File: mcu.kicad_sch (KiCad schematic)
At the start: 51 parts, among them IC3 RP2040, U1 W25Q64JVZPIQ, Y1 ABM3B-12.000MHZ-10-1-U-T

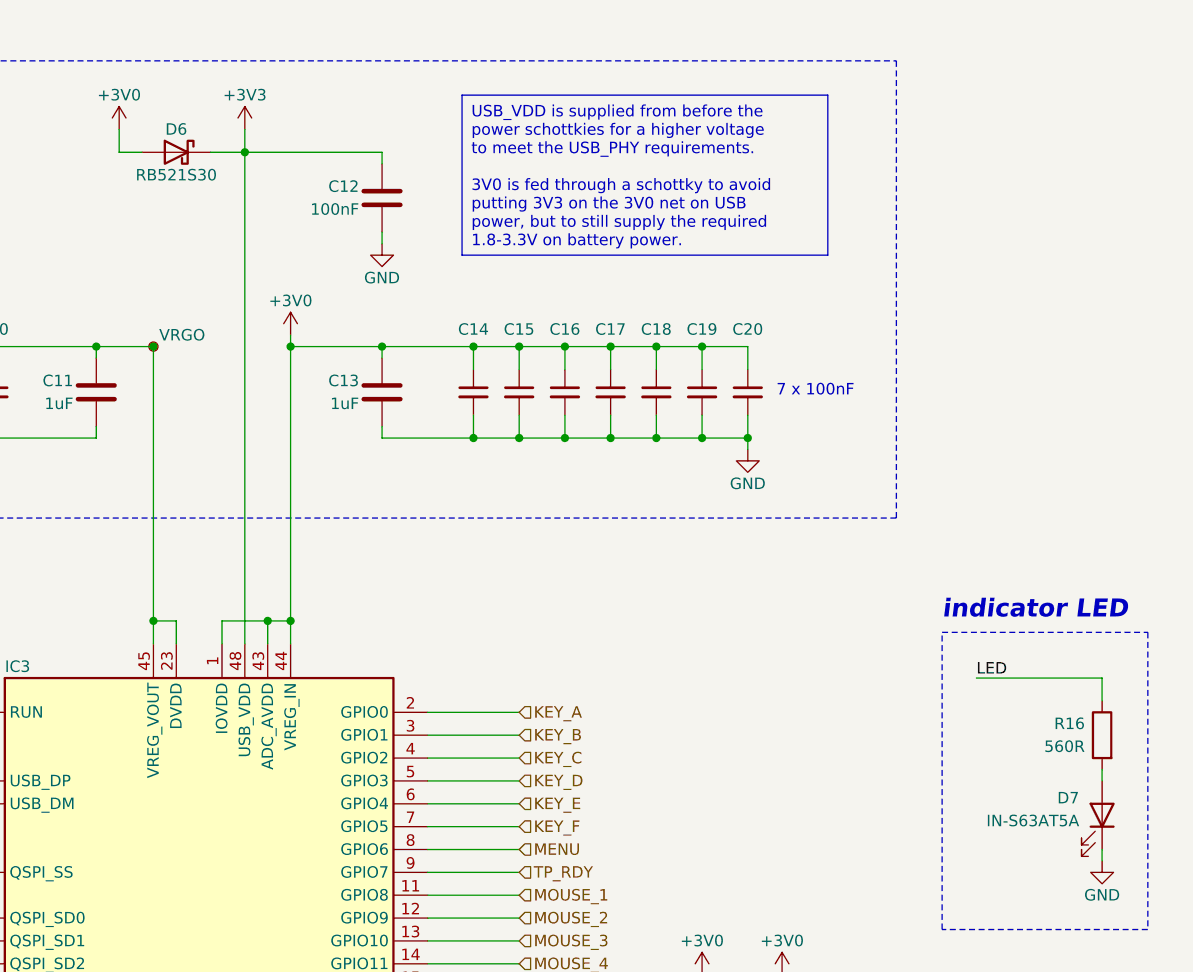
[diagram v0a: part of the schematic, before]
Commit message: add second battery TVS
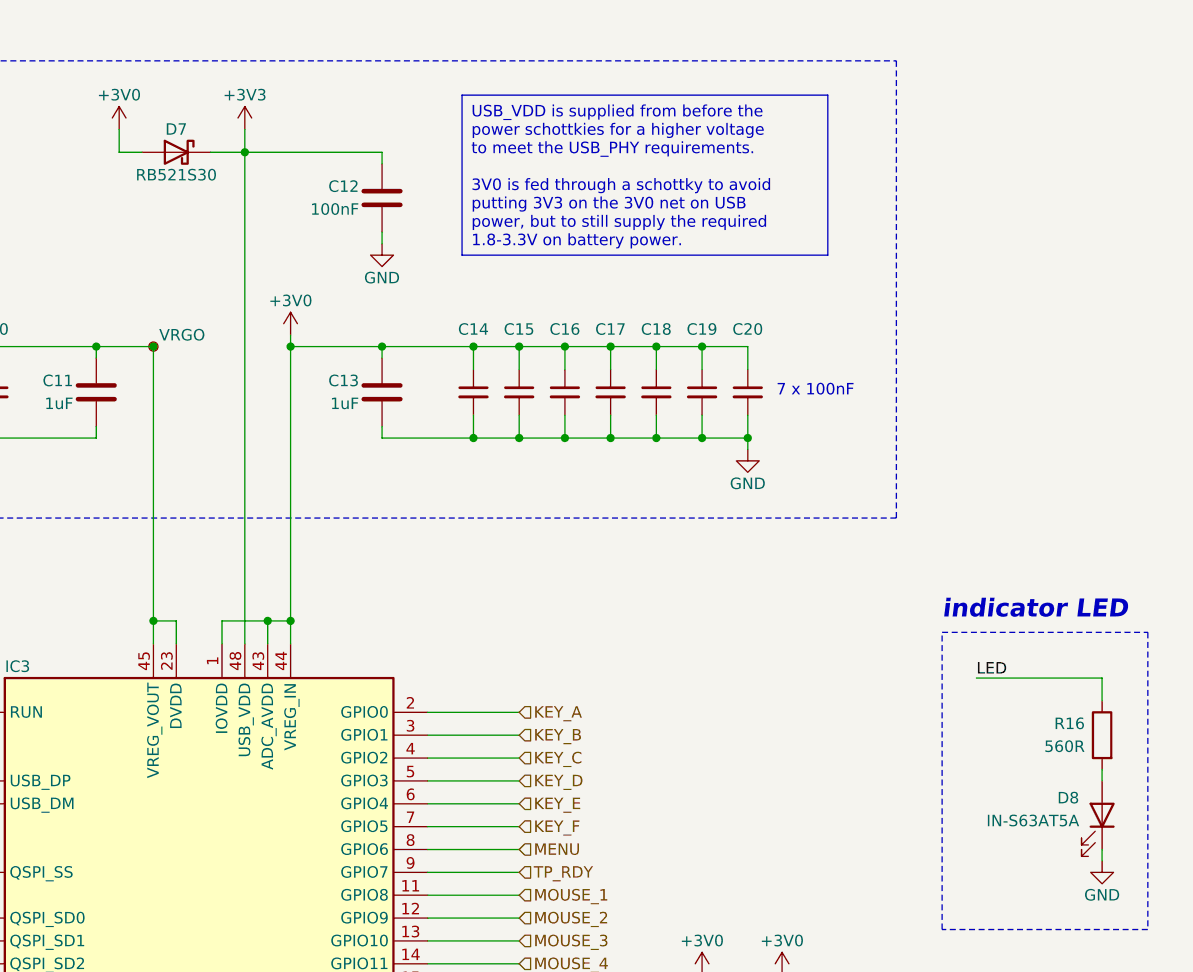
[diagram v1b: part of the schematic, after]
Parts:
- renumbered D6 to D7, D7 to D8
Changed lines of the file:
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@@
   (symbol (lib_id "user:RB521S30") (at 165.1 35.56 0) (mirror y) (unit 1)
     (in_bom yes) (on_board yes) (dnp no)
-    (property "Reference" "D6" (at 165.1 33.02 0)
+    (property "Reference" "D7" (at 165.1 33.02 0)
       (effects (font (size 1.27 1.27)))
     )
@@
       (project "gkos_pebble"
         (path "/ab6fff6e-44fa-4992-ab9d-8d9a7df4367d/b094ad32-9f85-443d-ad4d-e6b703944261"
-          (reference "D6") (unit 1)
+          (reference "D7") (unit 1)
         )
       )
@@
   (symbol (lib_id "Device:LED") (at 267.97 109.22 270) (mirror x) (unit 1)
     (in_bom yes) (on_board yes) (dnp no)
-    (property "Reference" "D7" (at 265.43 107.315 90)
+    (property "Reference" "D8" (at 265.43 107.315 90)
       (effects (font (size 1.27 1.27)) (justify right))
     )
@@
       (project "gkos_pebble"
         (path "/ab6fff6e-44fa-4992-ab9d-8d9a7df4367d/b094ad32-9f85-443d-ad4d-e6b703944261"
-          (reference "D7") (unit 1)
-        )
-      )
+          (reference "D8") (unit 1)
+        )
+      )

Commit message: add one more battery TVS
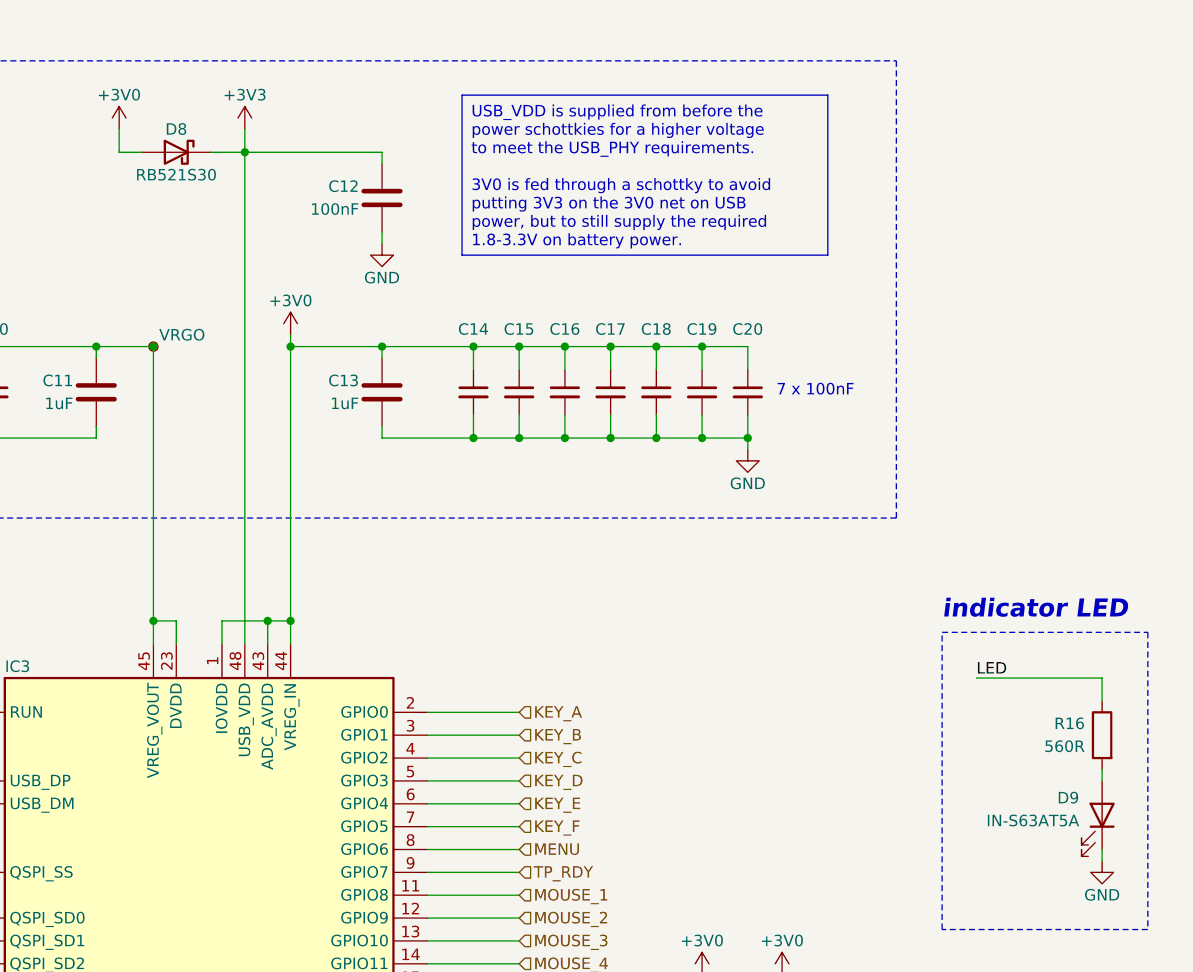
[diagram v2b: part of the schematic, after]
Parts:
- renumbered D7 to D8, D8 to D9
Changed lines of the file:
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@@
   (symbol (lib_id "user:RB521S30") (at 165.1 35.56 0) (mirror y) (unit 1)
     (in_bom yes) (on_board yes) (dnp no)
-    (property "Reference" "D7" (at 165.1 33.02 0)
+    (property "Reference" "D8" (at 165.1 33.02 0)
       (effects (font (size 1.27 1.27)))
     )
@@
       (project "gkos_pebble"
         (path "/ab6fff6e-44fa-4992-ab9d-8d9a7df4367d/b094ad32-9f85-443d-ad4d-e6b703944261"
-          (reference "D7") (unit 1)
+          (reference "D8") (unit 1)
         )
       )
@@
   (symbol (lib_id "Device:LED") (at 267.97 109.22 270) (mirror x) (unit 1)
     (in_bom yes) (on_board yes) (dnp no)
-    (property "Reference" "D8" (at 265.43 107.315 90)
+    (property "Reference" "D9" (at 265.43 107.315 90)
       (effects (font (size 1.27 1.27)) (justify right))
     )
@@
       (project "gkos_pebble"
         (path "/ab6fff6e-44fa-4992-ab9d-8d9a7df4367d/b094ad32-9f85-443d-ad4d-e6b703944261"
-          (reference "D8") (unit 1)
-        )
-      )
+          (reference "D9") (unit 1)
+        )
+      )

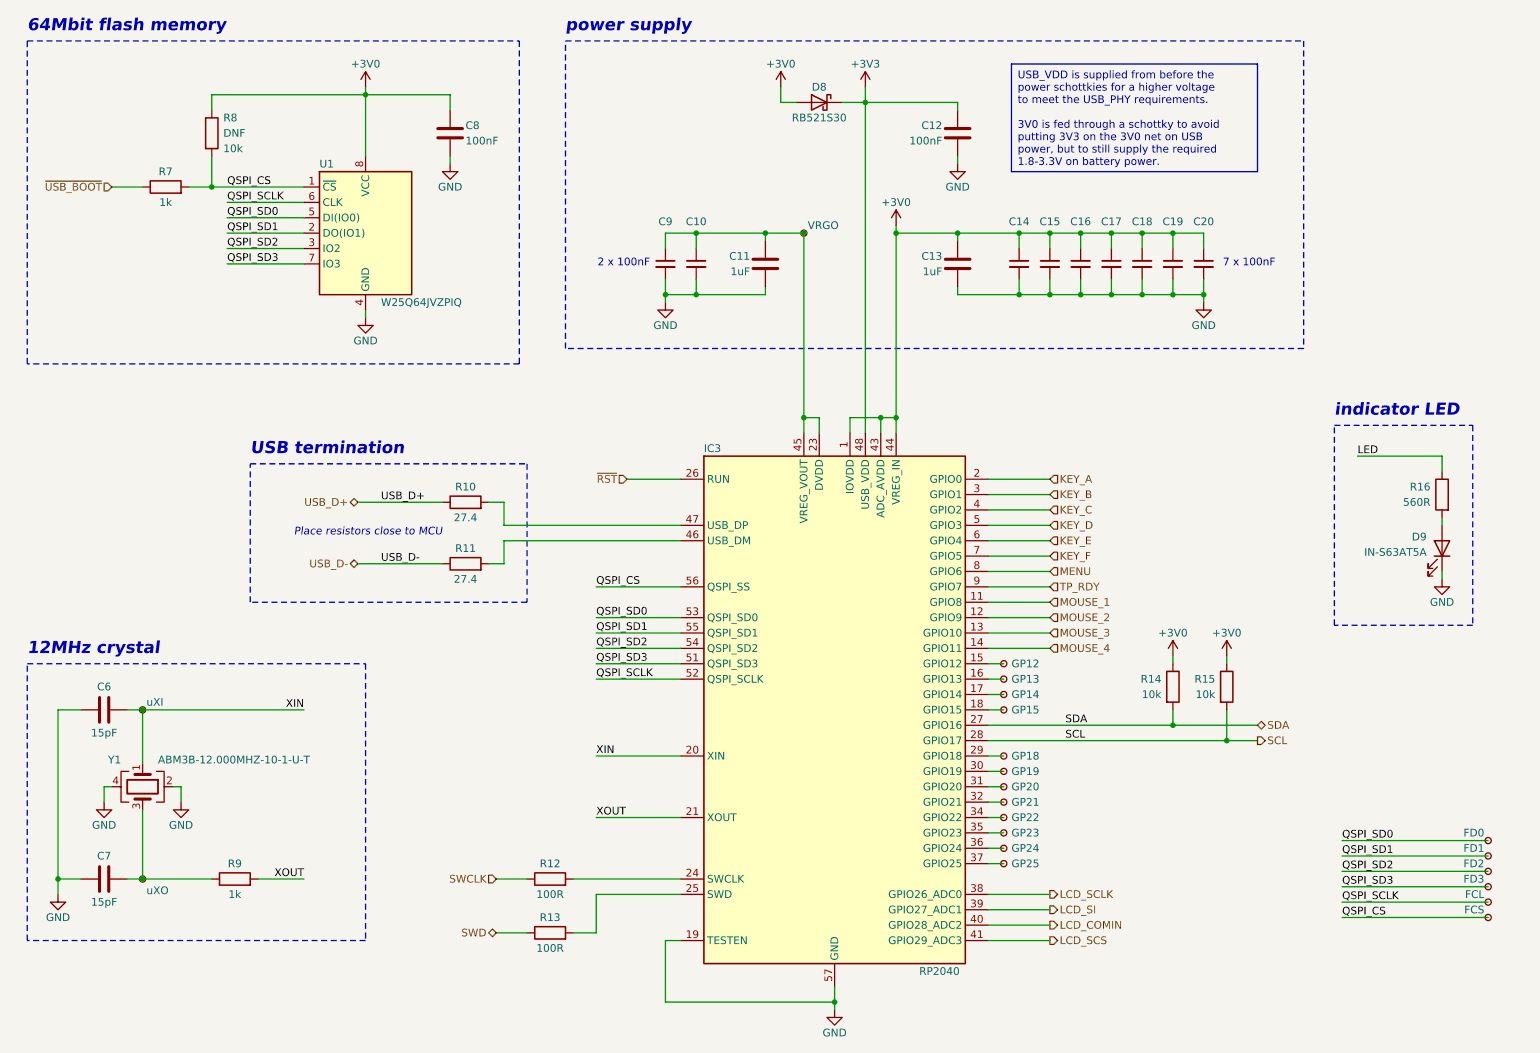
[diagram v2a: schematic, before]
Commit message: add the dang eeprom
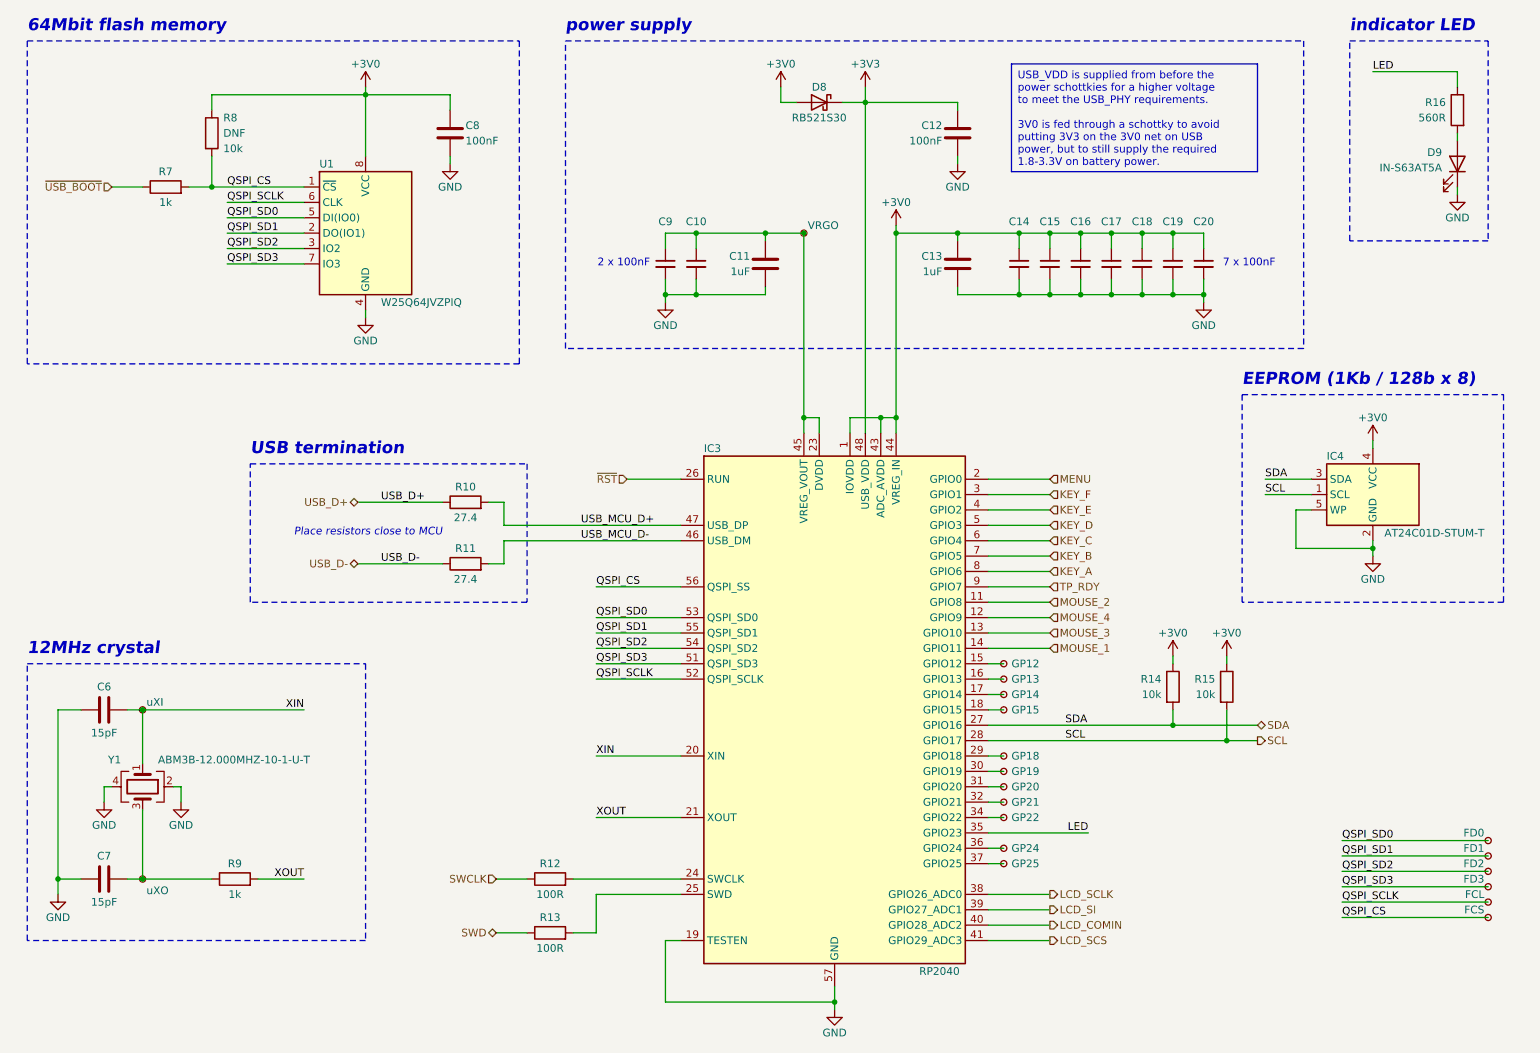
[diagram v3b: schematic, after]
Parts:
- removed TP40: GP23, TestPoint:TestPoint_Pad_D1.0mm, symbol Connector:TestPoint_Small
- added IC4: AT24C01D-STUM-T, Package_TO_SOT_SMD:SOT-23-5, symbol Memory_EEPROM:AT24CS01-STUM
- renumbered TP41 to TP40, TP42 to TP41, TP43 to TP42, TP44 to TP43, TP45 to TP44, TP46 to TP45, TP47 to TP46, TP48 to TP47
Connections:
- net +3V0: now also IC4.4 (VCC)
- net GND: now also IC4.2 (GND), IC4.5 (WP)
- net KEY_A: now also IC3.8 (GPIO6); no longer IC3.2 (GPIO0)
- net KEY_B: now also IC3.7 (GPIO5); no longer IC3.3 (GPIO1)
- net KEY_C: now also IC3.6 (GPIO4); no longer IC3.4 (GPIO2)
- net KEY_E: now also IC3.4 (GPIO2); no longer IC3.6 (GPIO4)
- net KEY_F: now also IC3.3 (GPIO1); no longer IC3.7 (GPIO5)
- net LED: now also IC3.35 (GPIO23)
- net MENU: now also IC3.2 (GPIO0); no longer IC3.8 (GPIO6)
- net MOUSE_1: now also IC3.14 (GPIO11); no longer IC3.11 (GPIO8)
- net MOUSE_2: now also IC3.11 (GPIO8); no longer IC3.12 (GPIO9)
- net MOUSE_4: now also IC3.12 (GPIO9); no longer IC3.14 (GPIO11)
- net SCL: now also IC4.1 (SCL)
- net SDA: now also IC4.3 (SDA)
- net USB_MCU_D+: now reaches IC3.47 (USB_DP), R10.2
- net USB_MCU_D-: now reaches IC3.46 (USB_DM), R11.2
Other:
- note added: "EEPROM (1Kb / 128b x 8)"
- moved on the sheet: D9, R16

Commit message: swap crystal for smaller one
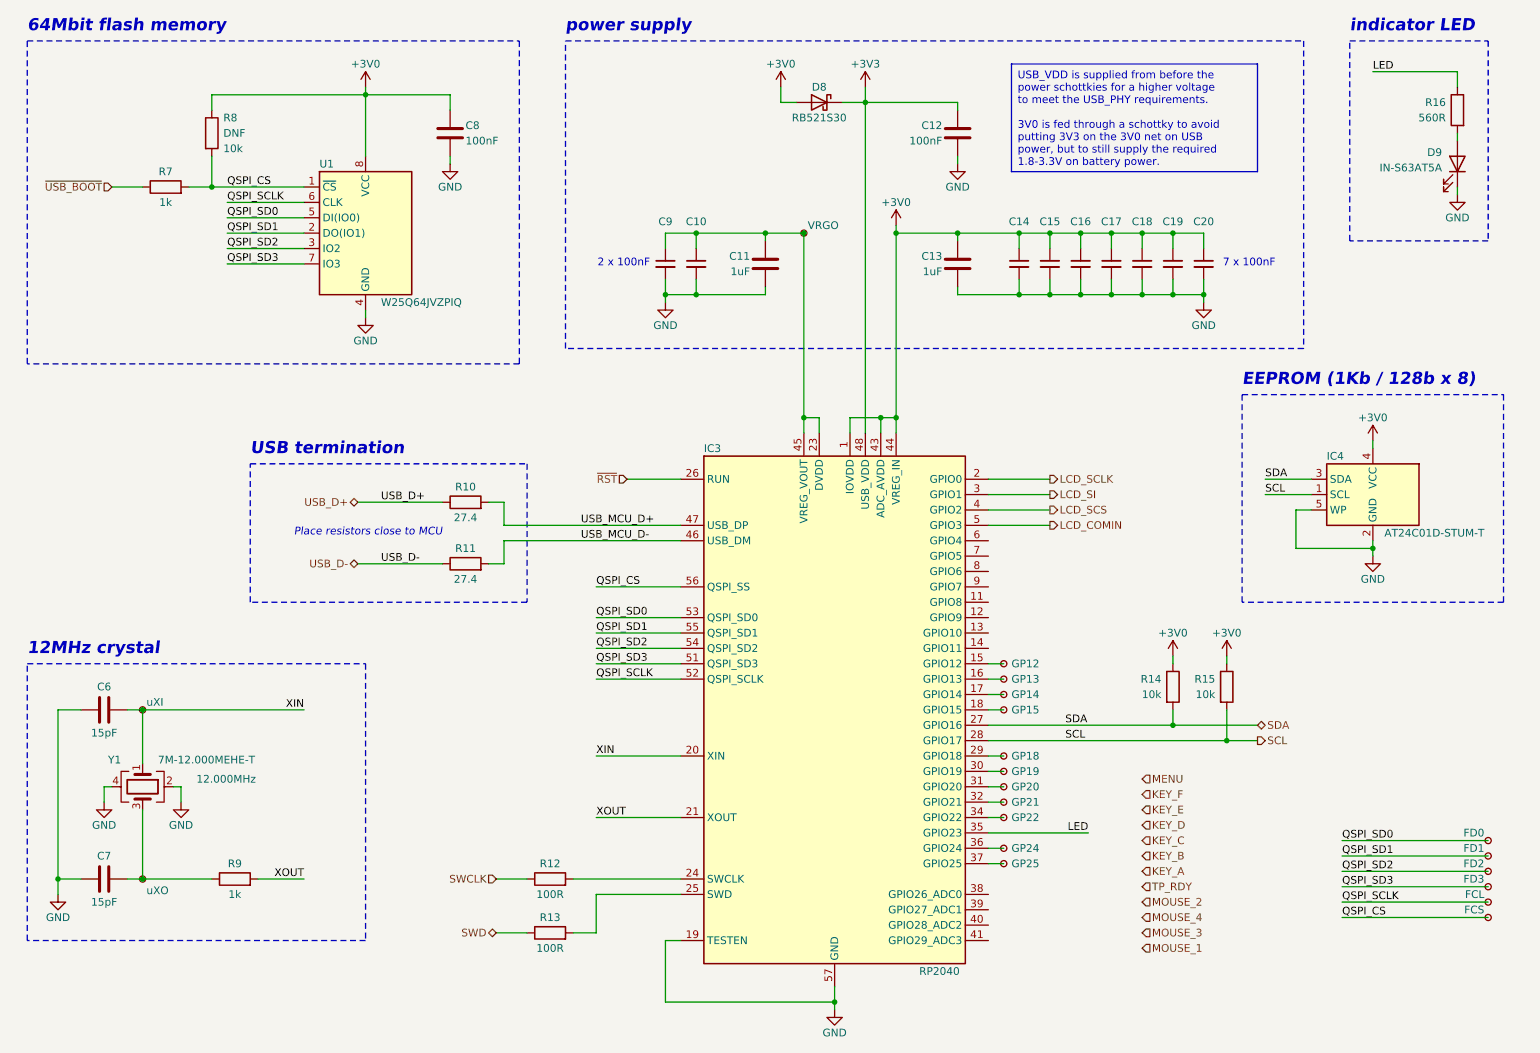
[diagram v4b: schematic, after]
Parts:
- C6, C7: footprint Capacitor_SMD:C_0603_1608Metric -> Capacitor_SMD:C_0402_1005Metric
- R9: footprint Resistor_SMD:R_0603_1608Metric -> Resistor_SMD:R_0402_1005Metric
- Y1: value ABM3B-12.000MHZ-10-1-U-T -> 7M-12.000MEHE-T; footprint Crystal:Crystal_SMD_Abracon_ABM3B-4Pin_5.0x3.2mm -> footprints:7M-12.000MEHE-T; Frequency (none) -> 12.000MHz
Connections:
- net KEY_A: no longer IC3.8 (GPIO6)
- net KEY_B: no longer IC3.7 (GPIO5)
- net KEY_C: no longer IC3.6 (GPIO4)
- net KEY_D: no longer IC3.5 (GPIO3)
- net KEY_E: no longer IC3.4 (GPIO2)
- net KEY_F: no longer IC3.3 (GPIO1)
- net LCD_COMIN: now also IC3.5 (GPIO3); no longer IC3.40 (GPIO28_ADC2)
- net LCD_SCLK: now also IC3.2 (GPIO0); no longer IC3.38 (GPIO26_ADC0)
- net LCD_SCS: now also IC3.4 (GPIO2); no longer IC3.41 (GPIO29_ADC3)
- net LCD_SI: now also IC3.3 (GPIO1); no longer IC3.39 (GPIO27_ADC1)
- net MENU: no longer IC3.2 (GPIO0)
- net MOUSE_1: no longer IC3.14 (GPIO11)
- net MOUSE_2: no longer IC3.11 (GPIO8)
- net MOUSE_3: no longer IC3.13 (GPIO10)
- net MOUSE_4: no longer IC3.12 (GPIO9)
- net TP_RDY: no longer IC3.9 (GPIO7)
